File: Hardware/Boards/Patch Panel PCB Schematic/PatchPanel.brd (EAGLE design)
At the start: 226 x 111.4 mm, 45 parts

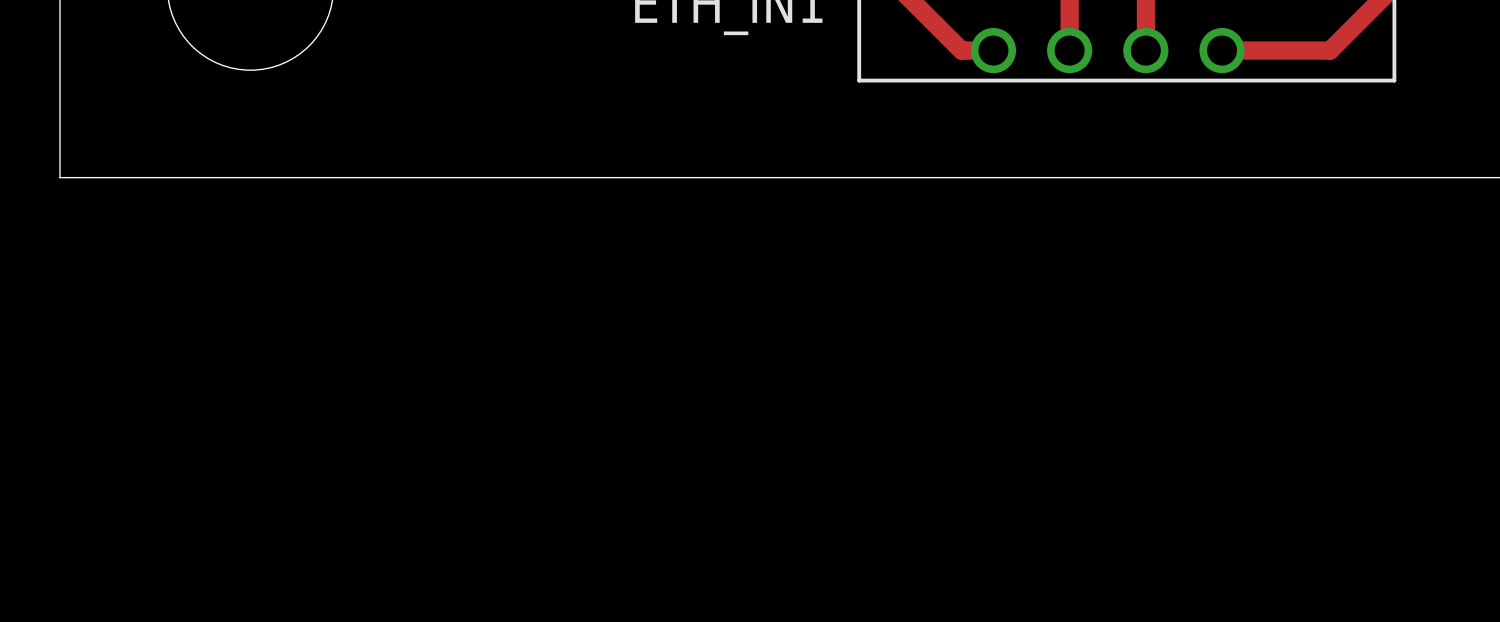
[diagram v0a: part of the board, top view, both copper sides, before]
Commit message: Made a few small changes. Board may still need a few connectors
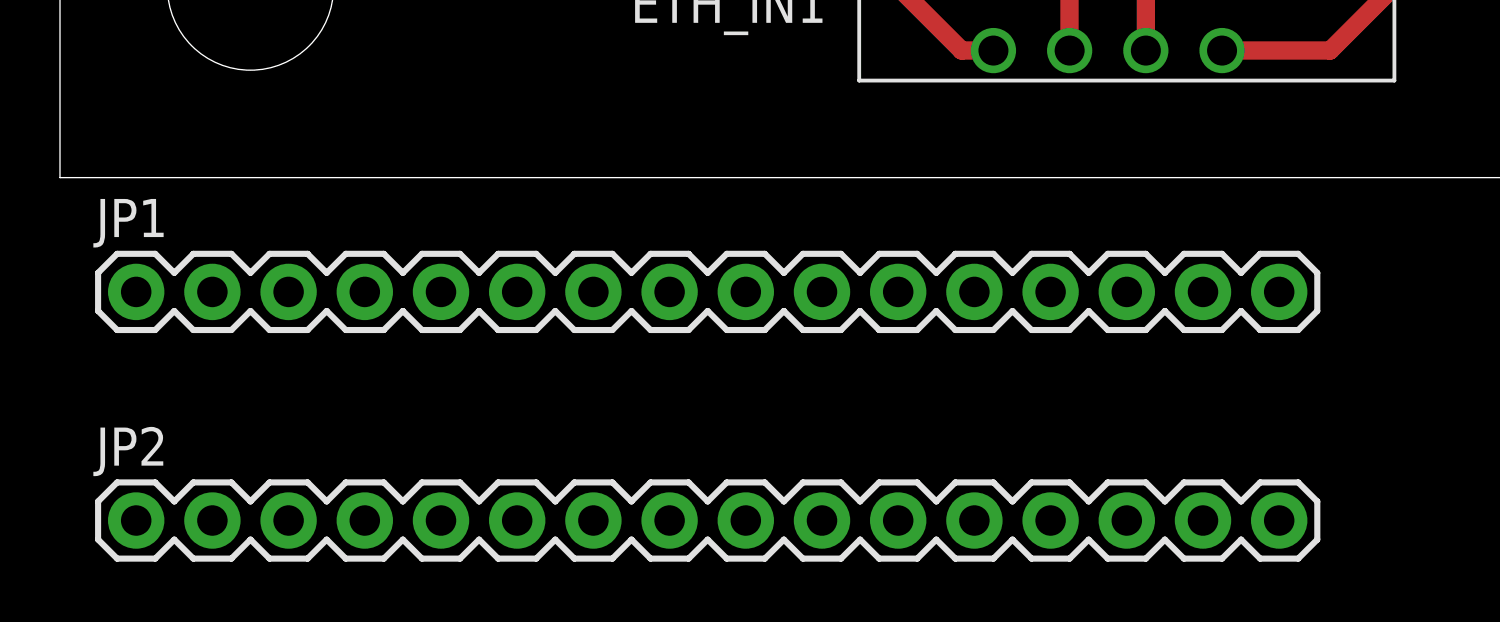
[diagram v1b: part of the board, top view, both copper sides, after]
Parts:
- added JP1, JP2: M16PTH, SparkFun-Connectors:1X16
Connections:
- new net N$61: JP1.1, JP2.16
- new net N$62: JP1.2, JP2.15
- new net N$63: JP1.3, JP2.14
- new net N$64: JP1.4, JP2.13
- new net N$65: JP1.5, JP2.12
- new net N$66: JP1.6, JP2.11
- new net N$67: JP1.7, JP2.10
- new net N$68: JP1.8, JP2.9
- new net N$69: JP1.9, JP2.8
- new net N$70: JP1.10, JP2.7
- new net N$71: JP1.11, JP2.6
- new net N$72: JP1.12, JP2.5
- new net N$73: JP1.13, JP2.4
- new net N$74: JP1.14, JP2.3
- new net N$75: JP1.15, JP2.2
- new net N$76: JP1.16, JP2.1
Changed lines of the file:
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@@
 <element name="12IN5" library="SparkFun-Connectors" package="SCREWTERMINAL-3.5MM-2" value="M023.5MM" x="212.09" y="30.48"/>
 <element name="12IN6" library="SparkFun-Connectors" package="SCREWTERMINAL-3.5MM-2" value="M023.5MM" x="212.09" y="62.23"/>
+<element name="JP1" library="SparkFun-Connectors" package="1X16" value="M16PTH" x="2.54" y="-3.81"/>
+<element name="JP2" library="SparkFun-Connectors" package="1X16" value="M16PTH" x="2.54" y="-11.43"/>
 </elements>
 <signals>
@@
 </polygon>
 </signal>
+<signal name="N$61">
+<contactref element="JP2" pad="16"/>
+<contactref element="JP1" pad="1"/>
+<wire x1="2.54" y1="-3.81" x2="40.64" y2="-11.43" width="0" layer="19" extent="1-1"/>
+</signal>
+<signal name="N$62">
+<contactref element="JP1" pad="2"/>
+<contactref element="JP2" pad="15"/>
+<wire x1="5.08" y1="-3.81" x2="38.1" y2="-11.43" width="0" layer="19" extent="1-1"/>
+</signal>
+<signal name="N$63">
+<contactref element="JP1" pad="3"/>
+<contactref element="JP2" pad="14"/>
+<wire x1="7.62" y1="-3.81" x2="35.56" y2="-11.43" width="0" layer="19" extent="1-1"/>
+</signal>
+<signal name="N$64">
+<contactref element="JP1" pad="4"/>
+<contactref element="JP2" pad="13"/>
+<wire x1="10.16" y1="-3.81" x2="33.02" y2="-11.43" width="0" layer="19" extent="1-1"/>
+</signal>
+<signal name="N$65">
+<contactref element="JP1" pad="5"/>
+<contactref element="JP2" pad="12"/>
+<wire x1="12.7" y1="-3.81" x2="30.48" y2="-11.43" width="0" layer="19" extent="1-1"/>
+</signal>
+<signal name="N$66">
+<contactref element="JP1" pad="6"/>
+<contactref element="JP2" pad="11"/>
+<wire x1="15.24" y1="-3.81" x2="27.94" y2="-11.43" width="0" layer="19" extent="1-1"/>
+</signal>
+<signal name="N$67">
+<contactref element="JP1" pad="7"/>
+<contactref element="JP2" pad="10"/>
+<wire x1="25.4" y1="-11.43" x2="17.78" y2="-3.81" width="0" layer="19" extent="1-1"/>
+</signal>
+<signal name="N$68">
+<contactref element="JP1" pad="8"/>
+<contactref element="JP2" pad="9"/>
+<wire x1="22.86" y1="-11.43" x2="20.32" y2="-3.81" width="0" layer="19" extent="1-1"/>
+</signal>
+<signal name="N$69">
+<contactref element="JP1" pad="9"/>
+<contactref element="JP2" pad="8"/>
+<wire x1="20.32" y1="-11.43" x2="22.86" y2="-3.81" width="0" layer="19" extent="1-1"/>
+</signal>
+<signal name="N$70">
+<contactref element="JP1" pad="10"/>
+<contactref element="JP2" pad="7"/>
+<wire x1="17.78" y1="-11.43" x2="25.4" y2="-3.81" width="0" layer="19" extent="1-1"/>
+</signal>
+<signal name="N$71">
+<contactref element="JP1" pad="11"/>
+<contactref element="JP2" pad="6"/>
+<wire x1="15.24" y1="-11.43" x2="27.94" y2="-3.81" width="0" layer="19" extent="1-1"/>
+</signal>
+<signal name="N$72">
+<contactref element="JP1" pad="12"/>
+<contactref element="JP2" pad="5"/>
+<wire x1="12.7" y1="-11.43" x2="30.48" y2="-3.81" width="0" layer="19" extent="1-1"/>
+</signal>
+<signal name="N$73">
+<contactref element="JP1" pad="13"/>
+<contactref element="JP2" pad="4"/>
+<wire x1="10.16" y1="-11.43" x2="33.02" y2="-3.81" width="0" layer="19" extent="1-1"/>
+</signal>
+<signal name="N$74">
+<contactref element="JP1" pad="14"/>
+<contactref element="JP2" pad="3"/>
+<wire x1="7.62" y1="-11.43" x2="35.56" y2="-3.81" width="0" layer="19" extent="1-1"/>
+</signal>
+<signal name="N$75">
+<contactref element="JP1" pad="15"/>
+<contactref element="JP2" pad="2"/>
+<wire x1="5.08" y1="-11.43" x2="38.1" y2="-3.81" width="0" layer="19" extent="1-1"/>
+</signal>
+<signal name="N$76">
+<contactref element="JP1" pad="16"/>
+<contactref element="JP2" pad="1"/>
+<wire x1="2.54" y1="-11.43" x2="40.64" y2="-3.81" width="0" layer="19" extent="1-1"/>
+</signal>
 </signals>

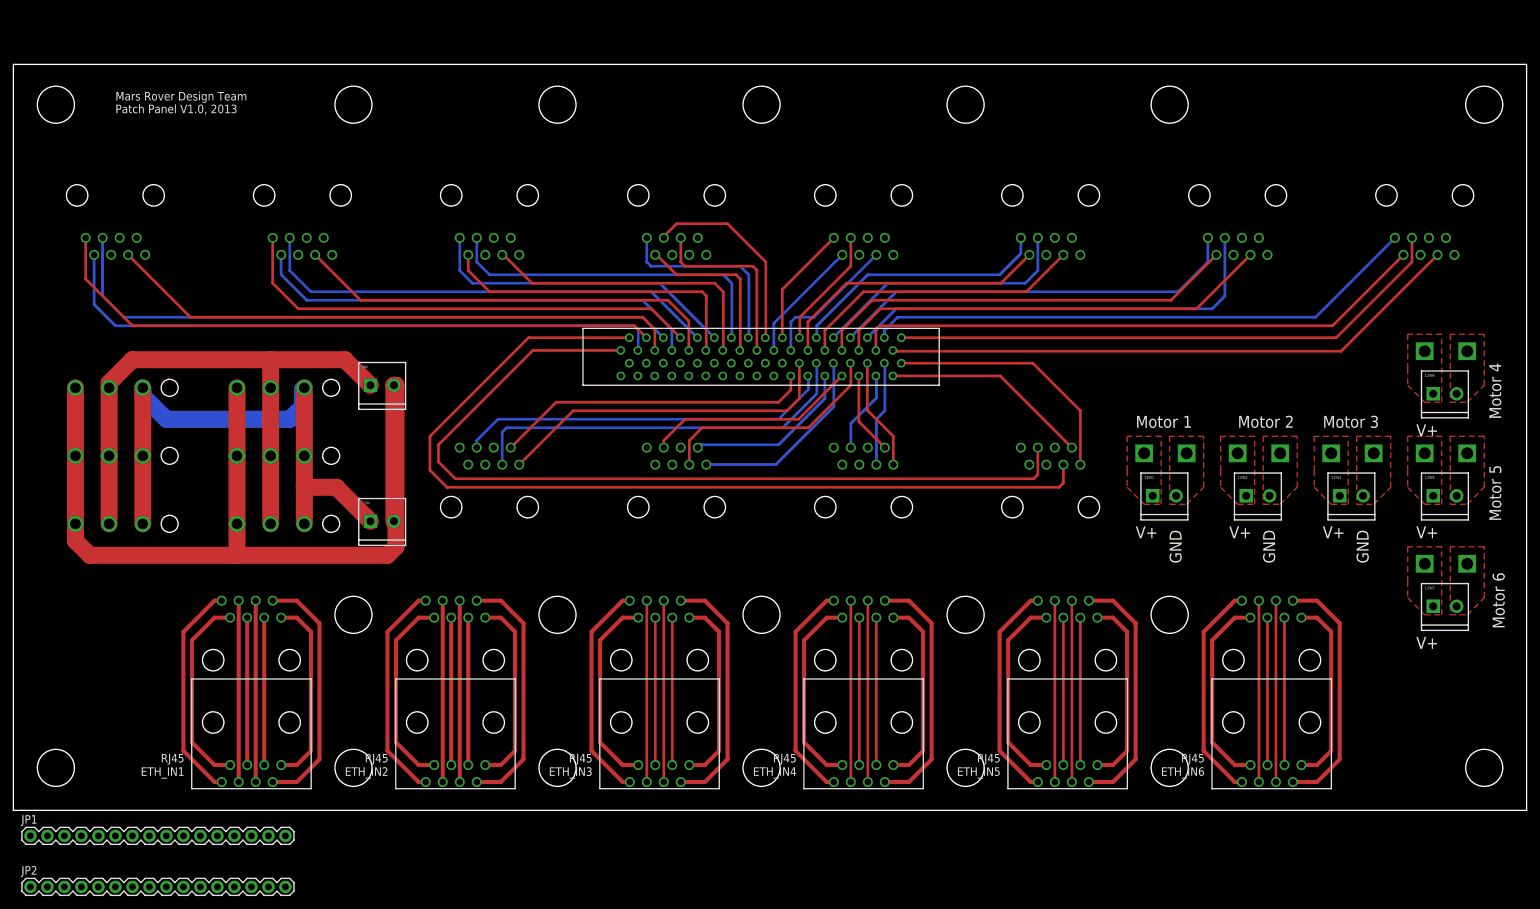
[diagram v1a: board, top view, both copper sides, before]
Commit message: Added antenna pass-throughs, lcd pass-through, clearance between motor connectors to patch panel.
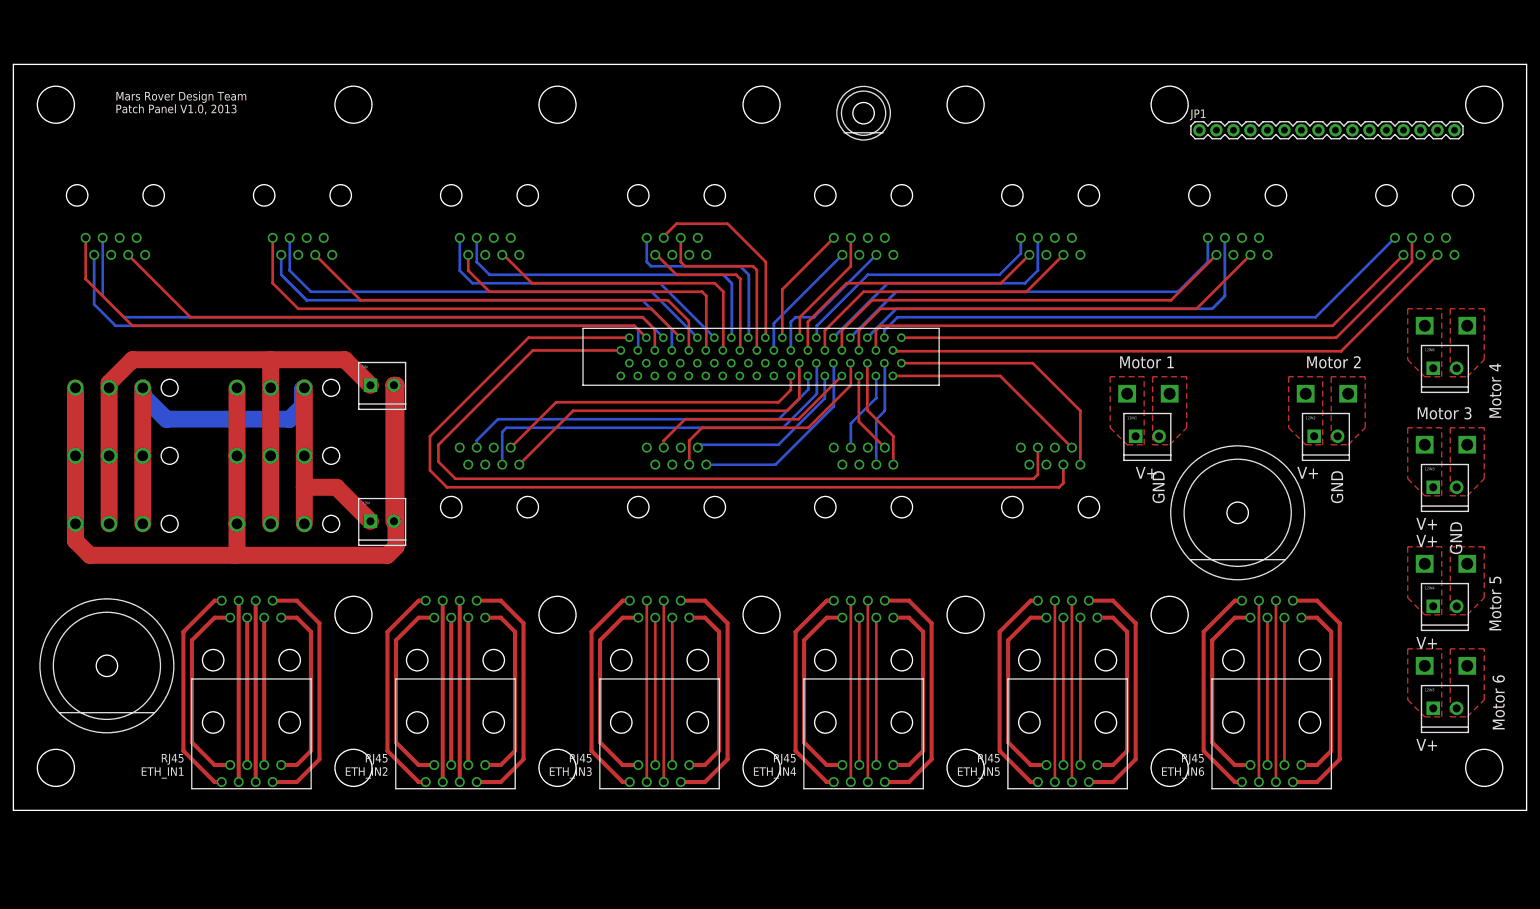
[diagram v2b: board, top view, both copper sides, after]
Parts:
- removed JP2: M16PTH, SparkFun-Connectors:1X16
- added U$14, U$15: N-TYPE-THRU, ant-pass-through:N-TYPE
- added U$16: SMA-THRU, ant-pass-through:SMA
- moved JP1 204.0 mm to (177.2, 101.6)
- moved U$11 16.5 mm to (217.2, 36.8)
- moved 12IN4 16.5 mm to (212.1, 30.5)
- moved 12IN5 15.2 mm to (212.1, 15.2)
- moved U$12 15.2 mm to (217.2, 21.6)
- moved 12IN3 14.0 mm to (212.1, 48.3)
- moved U$10 14.0 mm to (217.2, 54.6)
- moved 12IN2 13.5 mm to (194.3, 55.9)
- moved U$9 13.5 mm to (199.4, 62.2)
- moved 12IN1 9.25 mm to (167.6, 55.9)
- moved U$8 9.25 mm to (172.7, 62.2)
- moved 12IN6 3.81 mm to (212.1, 66.0)
- moved U$13 3.81 mm to (217.2, 72.4)
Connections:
- removed net N$61: JP1.1, JP2.16
- removed net N$62: JP1.2, JP2.15
- removed net N$63: JP1.3, JP2.14
- removed net N$64: JP1.4, JP2.13
- removed net N$65: JP1.5, JP2.12
- removed net N$66: JP1.6, JP2.11
- removed net N$67: JP1.7, JP2.10
- removed net N$68: JP1.8, JP2.9
- removed net N$69: JP1.9, JP2.8
- removed net N$70: JP1.10, JP2.7
- removed net N$71: JP1.11, JP2.6
- removed net N$72: JP1.12, JP2.5
- removed net N$73: JP1.13, JP2.4
- removed net N$74: JP1.14, JP2.3
- removed net N$75: JP1.15, JP2.2
- removed net N$76: JP1.16, JP2.1

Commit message: More patch panel updates for mechanical
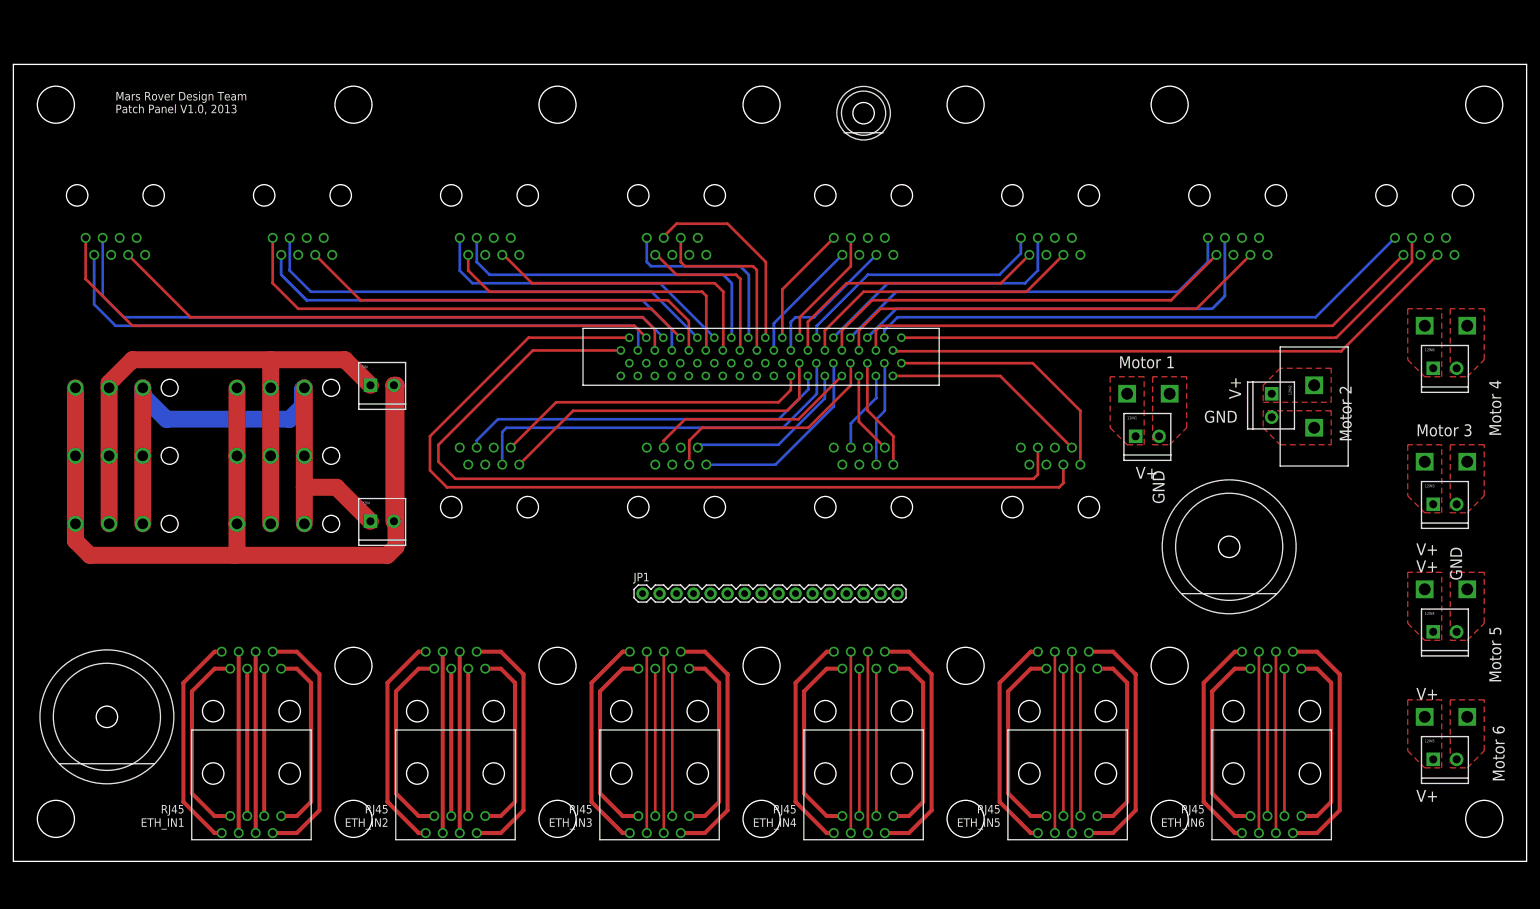
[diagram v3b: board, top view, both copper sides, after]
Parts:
- moved JP1 108.2 mm to (94.0, 32.4)
- moved 12IN2 8.98 mm to (188.0, 62.2), turned to 270 degrees
- moved 12IN5 7.62 mm to (212.1, 7.62)
- moved ETH_IN1 7.62 mm to (35.6, 3.81)
- moved ETH_IN2 7.62 mm to (66.0, 3.81)
- moved ETH_IN3 7.62 mm to (96.5, 3.81)
- moved ETH_IN4 7.62 mm to (127.0, 3.81)
- moved ETH_IN5 7.62 mm to (157.5, 3.81)
- moved ETH_IN6 7.62 mm to (188.0, 3.81)
- moved U$12 7.62 mm to (217.2, 14.0)
- moved U$14 7.62 mm to (14.0, 14.0)
- moved ETH_OUT1 7.62 mm to (35.6, 16.5)
- moved ETH_OUT2 7.62 mm to (66.0, 16.5)
- moved ETH_OUT3 7.62 mm to (96.5, 16.5)
- moved ETH_OUT4 7.62 mm to (127.0, 16.5)
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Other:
- board size 226 x 111.4 mm -> 226 x 119.1 mm

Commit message: fixed patch panel origin
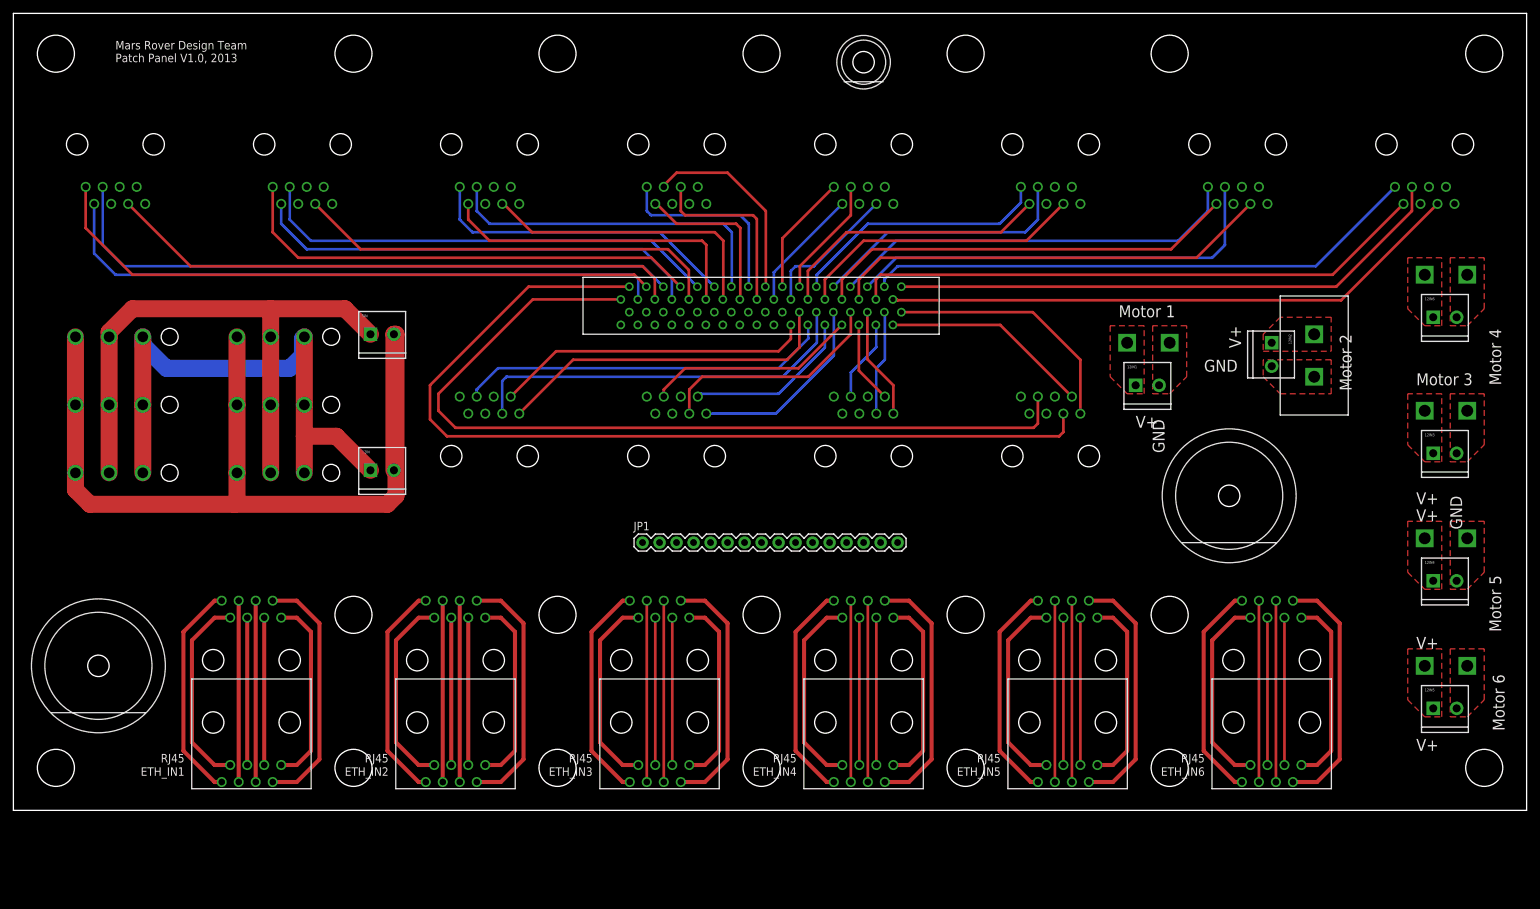
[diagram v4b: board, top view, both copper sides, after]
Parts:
- moved U$14 7.73 mm to (12.7, 21.6)
- moved 12IN3 7.62 mm to (212.1, 53.3)
- moved 5IN 7.62 mm to (53.3, 71.1)
- moved JP1 7.62 mm to (94.0, 40.0)
- moved RS-485_OUT1 7.62 mm to (210.8, 97.8)
- moved RS-485_OUT2 7.62 mm to (182.9, 97.8)
- moved RS-485_OUT3 7.62 mm to (154.9, 97.8)
- moved RS-485_OUT4 7.62 mm to (127.0, 97.8)
- moved RS-485_OUT5 7.62 mm to (99.1, 97.8)
- moved RS-485_OUT6 7.62 mm to (71.1, 97.8)
- moved RS-485_OUT7 7.62 mm to (43.2, 97.8)
- moved RS-485_OUT8 7.62 mm to (15.2, 97.8)
- moved U$1 7.62 mm to (85.1, 71.1)
- moved U$13 7.62 mm to (217.2, 80.0)
- moved U$15 7.62 mm to (181.6, 47.0)
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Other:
- board size 226 x 119.1 mm -> 226 x 119 mm
